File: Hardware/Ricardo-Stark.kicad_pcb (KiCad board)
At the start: 4 copper layers, 124 x 56 mm, 336 parts, among them IC1 TPS61089RNRR, IC2 AP2205-W5-7, IC3 AP2205-W5-7, IC4 TPS61089RNRR, J1 RBUS, J10 1053131104, J11 Conn_01x08_Socket, J12 Conn_01x02_Male, J13 1053131104, J14 Conn_01x02_Male, J15 Conn_01x02_Male, J16 Conn_01x07_Socket, J17 ServoCH1, J18 ServoCH2, J2 USB_C_Receptacle_USB2.0, J3 ST1W008S4TR2000, J5 Conn_01x03_Socket, J6 1053131104, J7 1053131104, J8 1053131104, J9 1053131104, Q7 BSZ025N04LS, Q8 BSZ025N04LS, Q9 BSZ025N04LS, U1 ESP32-S3, U10 SiC438BED-T1-GE3, U11 782-TCMT1109, U12 INA219AxDCN, U13 MAX31856, U14 PCA9534RGVR, U15 782-TCMT1109, U2 SN65HVD230, U3 LM66200DRLR, U4 MAX77827AEFD+T, U5 SC4215, U6 SiC437BED-T1-GE3, U7 ADS131M06IPBS, U8 PCA9685BS, U9 782-TCMT1109, Y1 R940000171

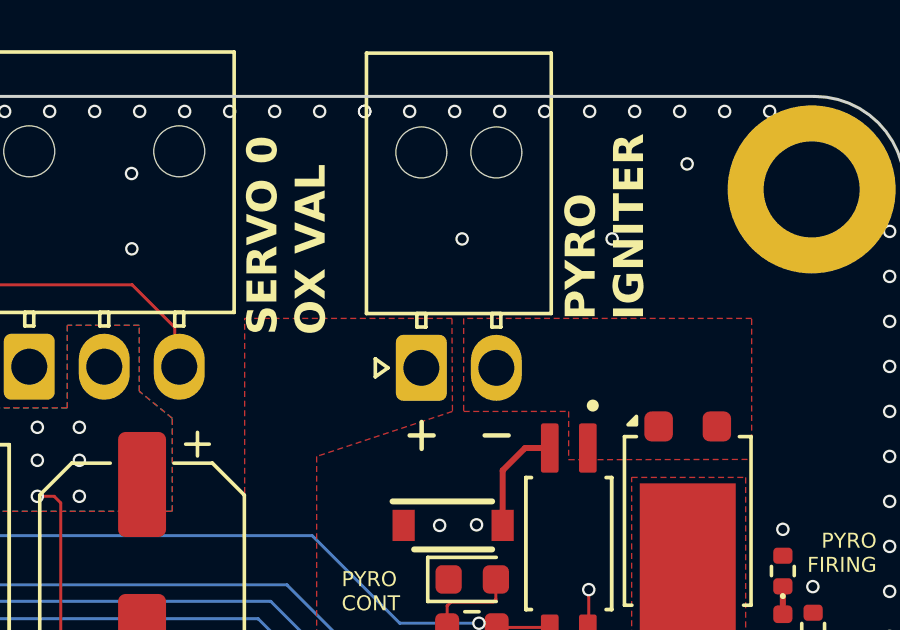
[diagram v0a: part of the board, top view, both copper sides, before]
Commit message: Added flyback on pyro channel
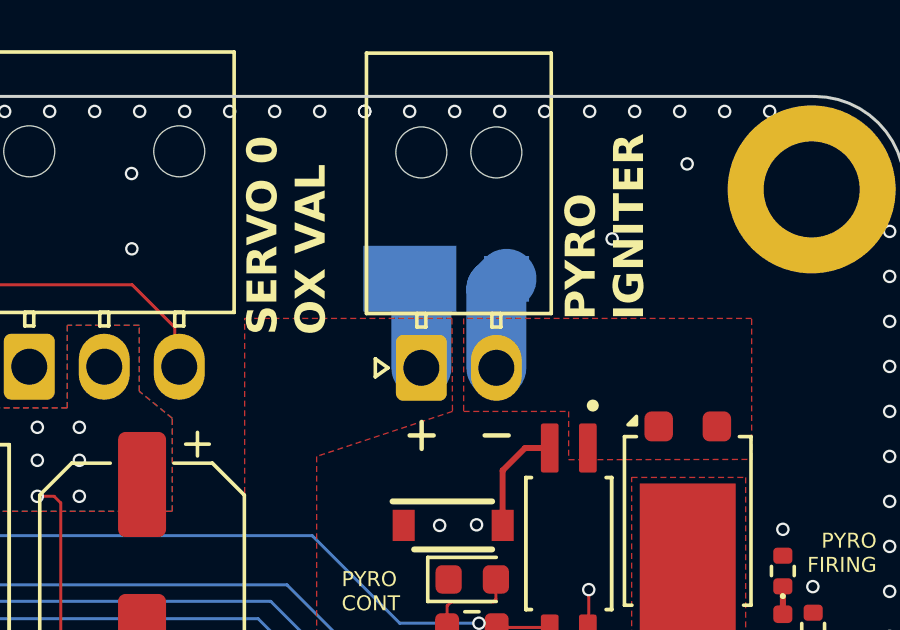
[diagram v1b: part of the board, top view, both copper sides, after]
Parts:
- added D18: V8PAM10S-M3/I, iclr:V8PAM10SM3I, B.Cu at (220.6, 67.1)
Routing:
- net /Pyro/PyroV: track 4.40 -> 7.52 mm
- net Net-(D18-A): track 0.00 -> 3.11 mm
- net GND: vias 503 -> 502
